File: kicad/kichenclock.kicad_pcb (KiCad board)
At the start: 2 copper layers, 46.5 x 30.4 mm, 19 parts, among them CON1 AVR-ISP-6, J1 pwr_1v5, J2 OLED_DISPLAY, SW1 DOWN, SW2 OK, SW3 UP, U1 LT1073, U2 ATTINY85-20SU

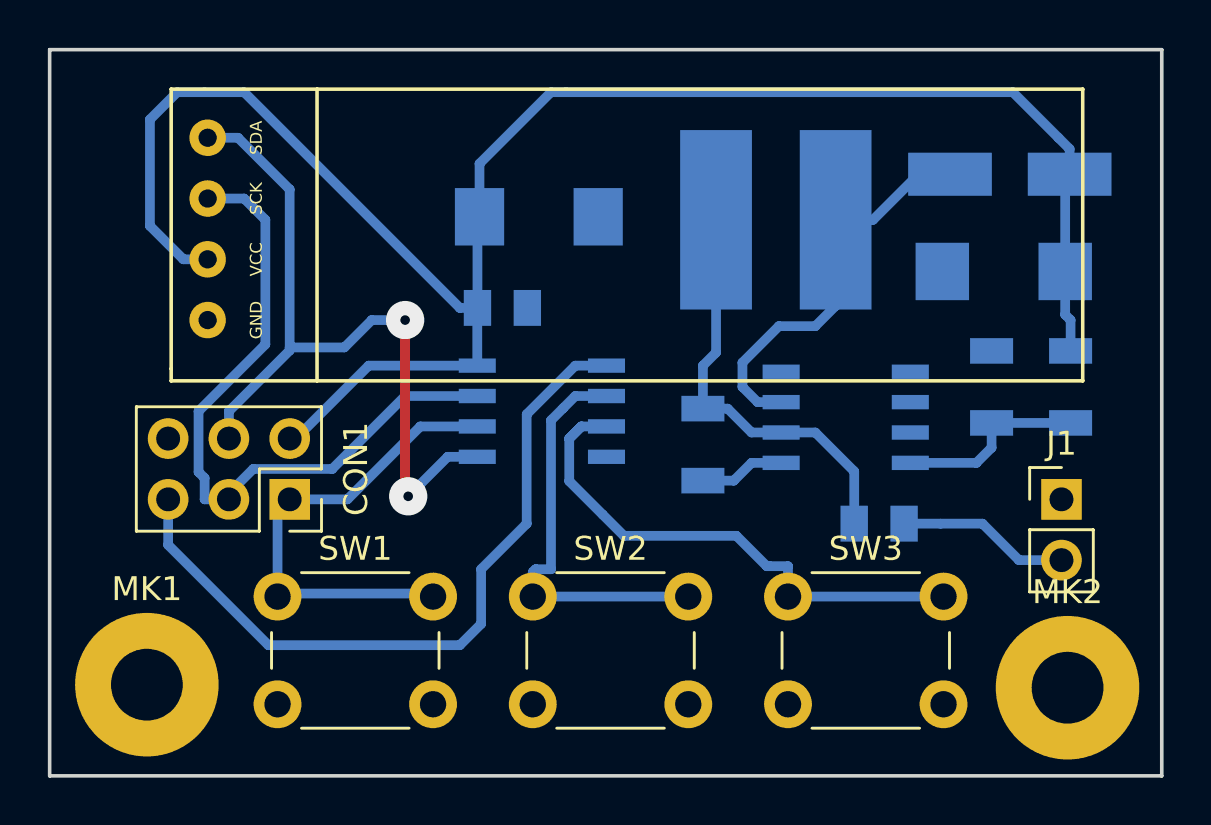
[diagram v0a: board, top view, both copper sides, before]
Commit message: change the most path to 20 mil
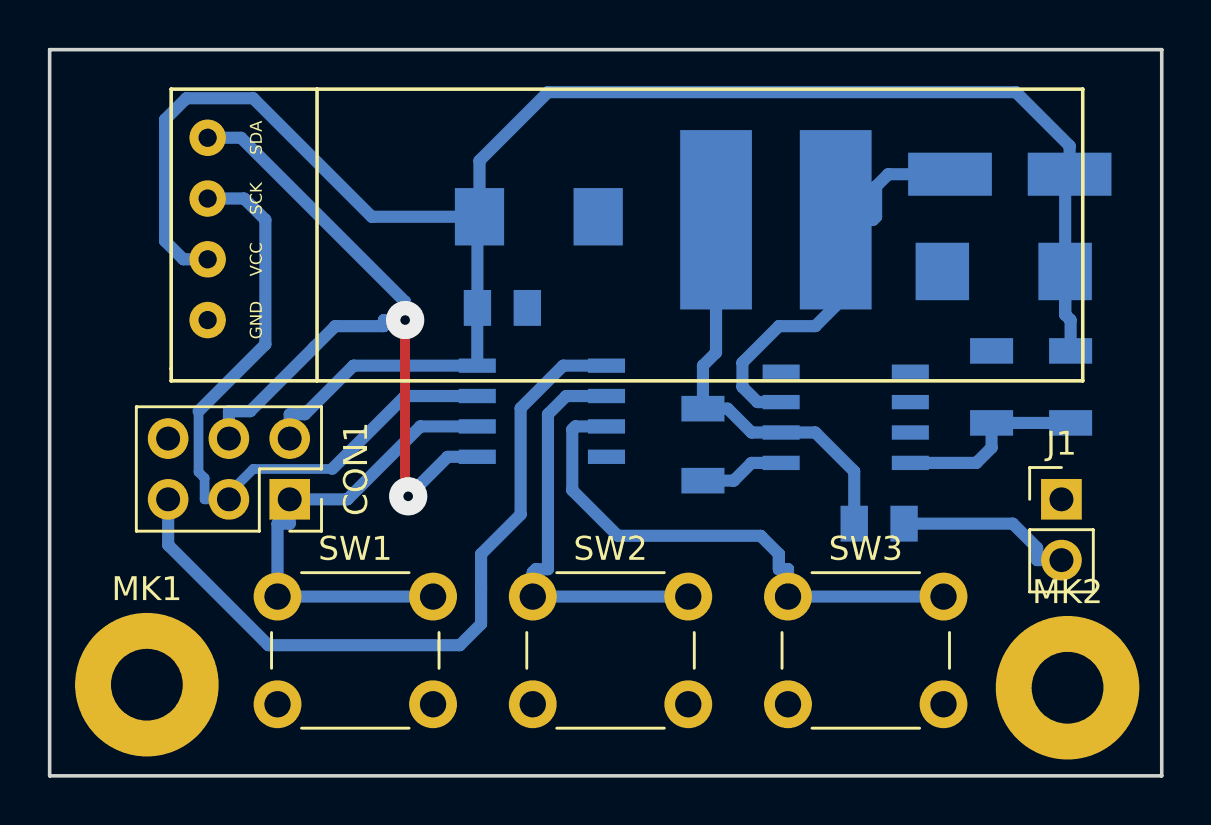
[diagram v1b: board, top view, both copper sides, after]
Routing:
- net /MISO: track 19.9 -> 26.9 mm
- net Net-(SW2-Pad1): track 17.5 -> 18.8 mm
- net +3V3: track 77.9 -> 79.2 mm
- net /MOSI: track 32.1 -> 33.1 mm
- net Net-(SW3-Pad1): track 22.7 -> 23.4 mm
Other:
- net class pwr added: clearance 0.2, trace_width 0.508, via_dia 0.8, via_drill 0.4
